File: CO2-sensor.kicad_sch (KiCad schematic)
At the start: 41 parts, among them IC1 SCD41-D-R1, IC2 NCP1117ST33T3G, IC3 W25Q32JVSSIQ, J1 1734028-1, U1 RP2040, Y1 ABM8-272-T3

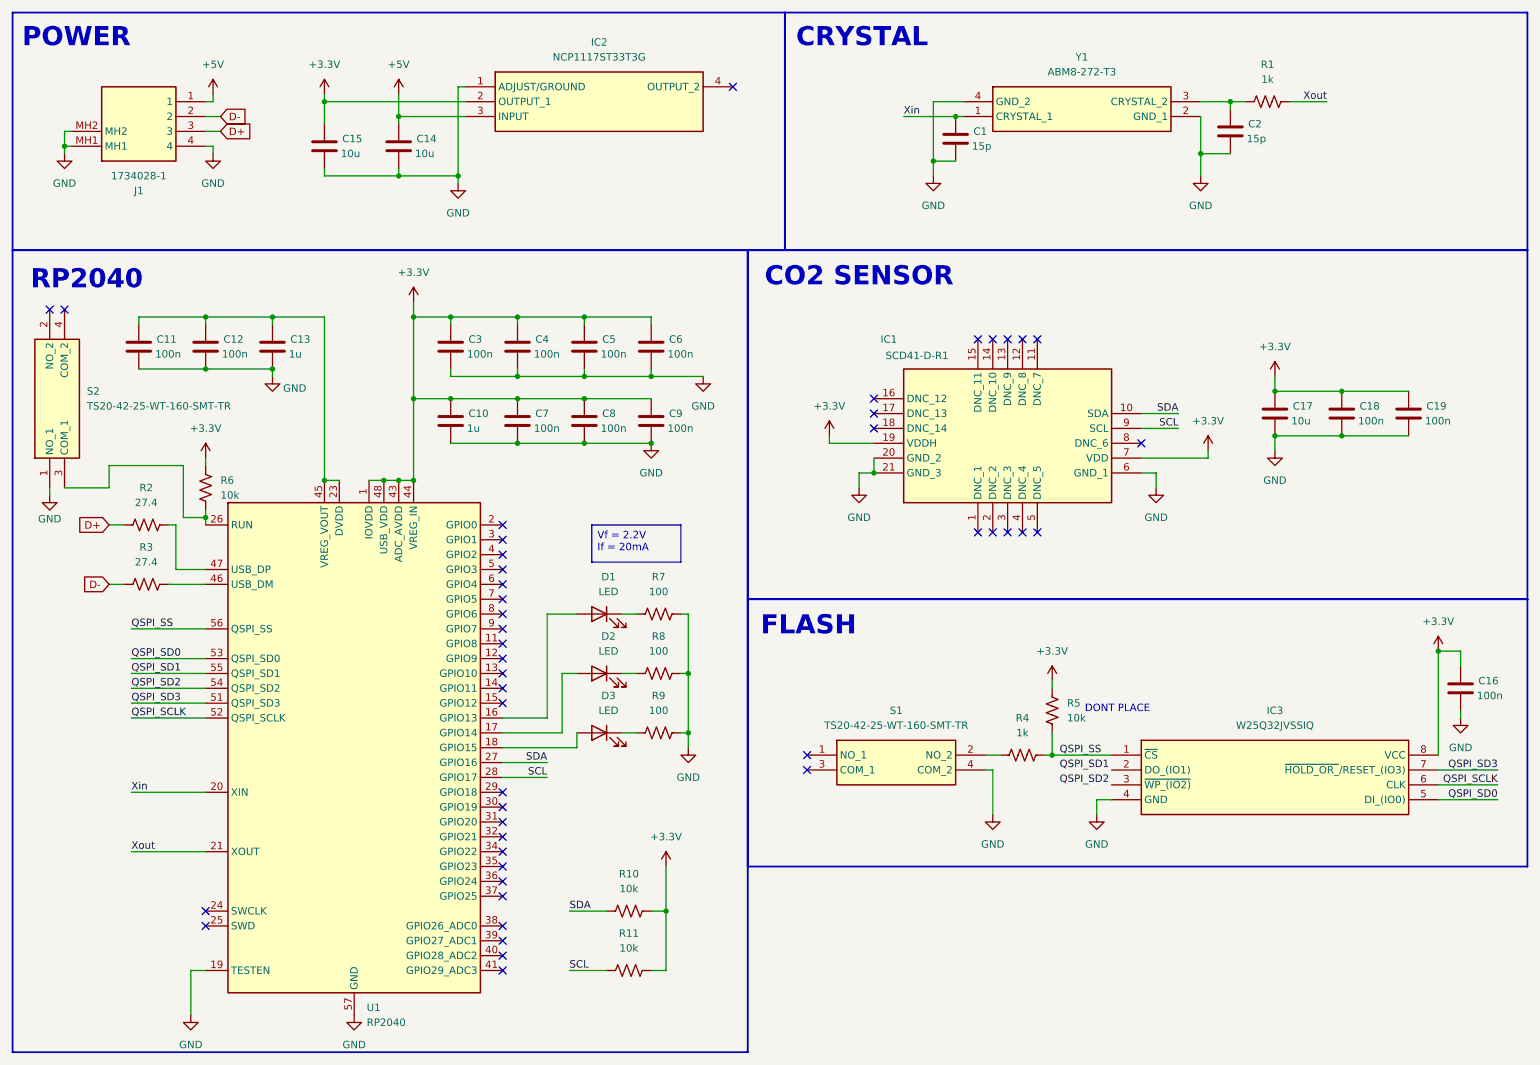
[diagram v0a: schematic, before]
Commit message: removed components folder
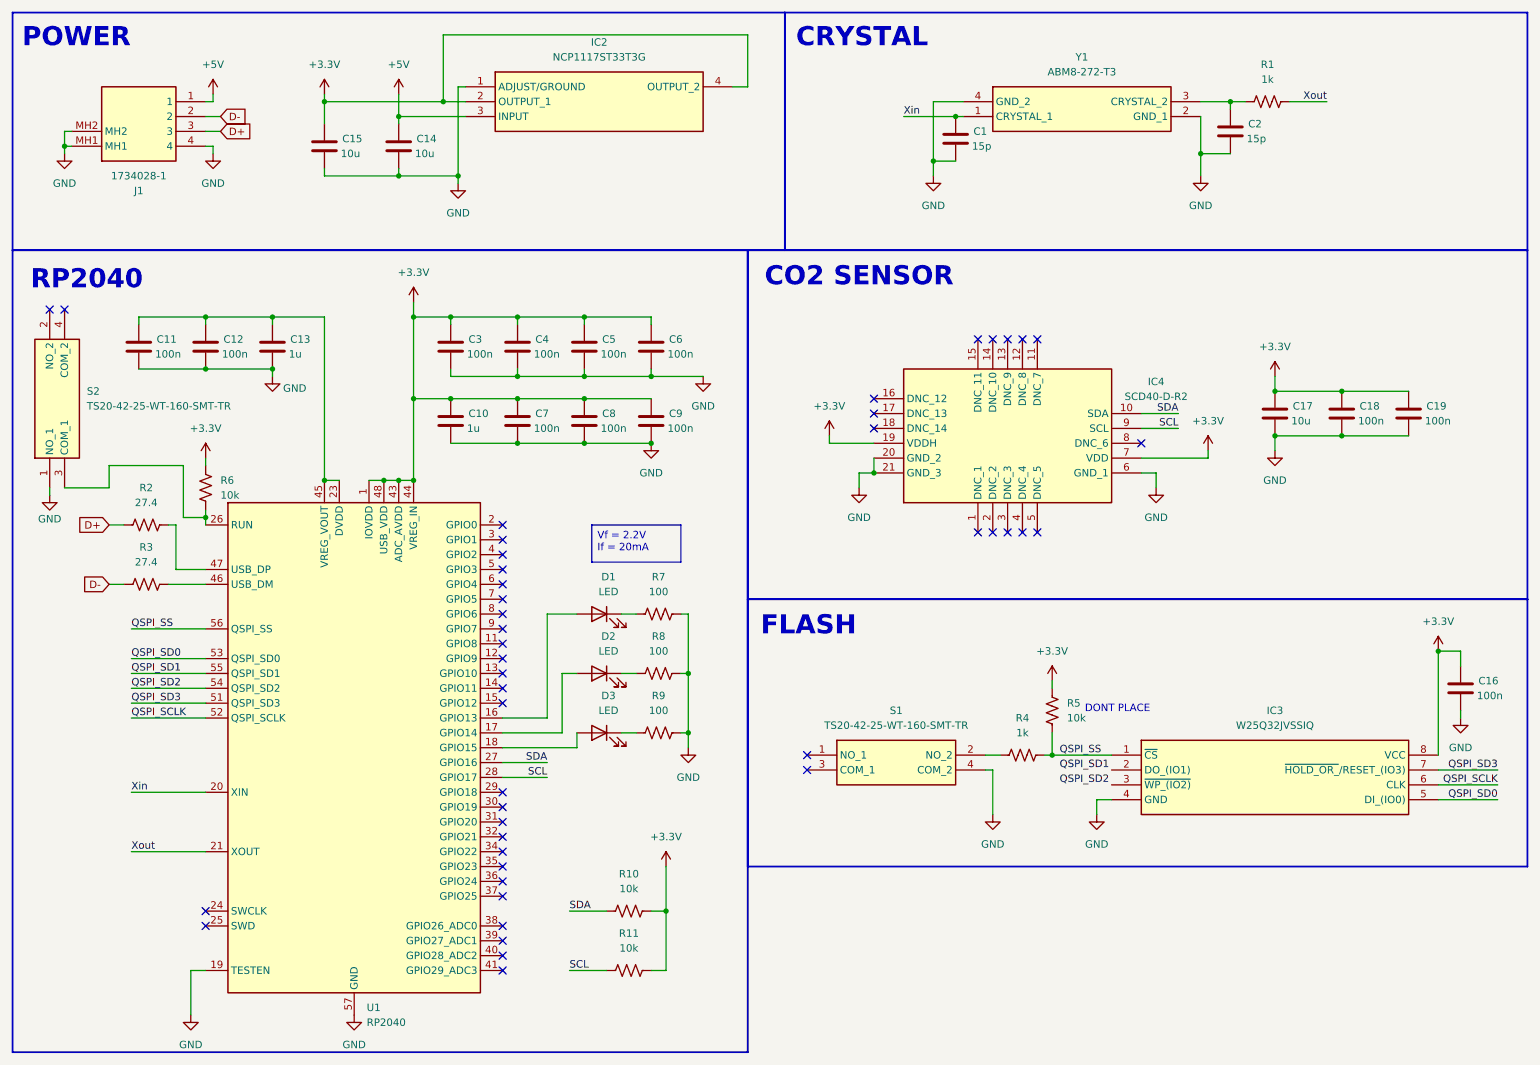
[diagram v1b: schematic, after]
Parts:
- removed IC1: SCD41-D-R1, SCD41DR1, symbol Imported_parts:SCD41-D-R1
- added IC4: SCD40-D-R2, SCD40DR2, symbol Imported_parts:SCD40-D-R2
- C10, C11, C12, C13, C16, C18, C19, C3, C4, C5, C6, C7, C8, C9: footprint Capacitor_SMD:C_01005_0402Metric -> Capacitor_SMD:C_0402_1005Metric
- R10, R11: footprint Resistor_SMD:R_0402_1005Metric -> Resistor_SMD:R_0603_1608Metric
- R5, R6: footprint Resistor_SMD:R_0201_0603Metric -> Resistor_SMD:R_0603_1608Metric
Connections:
- net +3.3V: now also IC2.4 (OUTPUT_2), R10.1, R11.1, IC4.19 (VDDH), IC4.7 (VDD); no longer R10.2, R11.2
- net GND: now also IC4.20 (GND_2), IC4.21 (GND_3), IC4.6 (GND_1)
- net SCL: now also R11.2, IC4.9 (SCL); no longer R11.1
- net SDA: now also R10.2, IC4.10 (SDA); no longer R10.1
- no-connect marks 46 -> 45
